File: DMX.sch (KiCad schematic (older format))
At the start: 7 parts, among them U10 ST485CDR

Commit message: Replaced the 10k-Resistor with one that is in stock
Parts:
- R25, R26: Buy https://www.digikey.com/product-detail/en/yageo/RC0603FR-07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 -> https://www.digikey.com/product-detail/en/bourns-inc/CR0603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
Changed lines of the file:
@@
 F 2 "Resistor_SMD:R_0603_1608Metric" V 980 2650 50  0001 C CNN
 F 3 "" H 1050 2650 50  0001 C CNN
-F 4 "https://www.digikey.com/product-detail/en/yageo/RC0603FR-0710KL/311-10.0KHRCT-ND/729827" V 1050 2650 50  0001 C CNN "Buy"
+F 4 "https://www.digikey.com/product-detail/en/bourns-inc/CR0603-FX-1002HLF/CR0603-FX-1002HLFCT-ND/3925297" V 1050 2650 50  0001 C CNN "Buy"
 	1    1050 2650
 	1    0    0    -1
@@
 F 2 "Resistor_SMD:R_0603_1608Metric" V 1680 2650 50  0001 C CNN
 F 3 "" H 1750 2650 50  0001 C CNN
-F 4 "https://www.digikey.com/product-detail/en/yageo/RC0603FR-0710KL/311-10.0KHRCT-ND/729827" V 1750 2650 50  0001 C CNN "Buy"
+F 4 "https://www.digikey.com/product-detail/en/bourns-inc/CR0603-FX-1002HLF/CR0603-FX-1002HLFCT-ND/3925297" V 1750 2650 50  0001 C CNN "Buy"
 	1    1750 2650
 	1    0    0    -1

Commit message: Replaced the 100nF Low-Voltage-Caps with one, which is still in stock
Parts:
- C34: Buy https://www.digikey.com/product-detail/en/kemet/C0603C104K3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 -> https://www.digikey.com/product-detail/en/murata-electronic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
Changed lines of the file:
@@
 F 2 "Capacitor_SMD:C_0603_1608Metric" H 2400 1400 50  0001 C CNN
 F 3 "" H 2400 1400 50  0001 C CNN
-F 4 "https://www.digikey.com/product-detail/en/kemet/C0603C104K3RACTU/399-1281-1-ND/416057" V 2400 1400 50  0001 C CNN "Buy"
+F 4 "https://www.digikey.com/product-detail/en/murata-electronics-north-america/GCM188R71C104KA37D/490-4774-1-ND/1641693" V 2400 1400 50  0001 C CNN "Buy"
 	1    2400 1400
 	0    1    1    0

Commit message: Removed the LV-Caps with the HV-Caps to remain consistent
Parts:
- C34: footprint Capacitor_SMD:C_0603_1608Metric -> Capacitor_SMD:C_0805_2012Metric; Buy https://www.digikey.com/product-detail/en/murata-electronics-north-america/GCM188R71C104KA37D/490-4774-1-ND/1641693 -> https://www.digikey.com/product-detail/en/murata-electronics-north-america/GCM21BR72A104KA37L/490-4789-1-ND/1641708
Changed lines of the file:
@@
 F 0 "C34" V 2500 1350 50  0000 L CNN
 F 1 "100nF" V 2300 1300 50  0000 L CNN
-F 2 "Capacitor_SMD:C_0603_1608Metric" H 2400 1400 50  0001 C CNN
+F 2 "Capacitor_SMD:C_0805_2012Metric" H 2400 1400 50  0001 C CNN
 F 3 "" H 2400 1400 50  0001 C CNN
-F 4 "https://www.digikey.com/product-detail/en/murata-electronics-north-america/GCM188R71C104KA37D/490-4774-1-ND/1641693" V 2400 1400 50  0001 C CNN "Buy"
+F 4 "https://www.digikey.com/product-detail/en/murata-electronics-north-america/GCM21BR72A104KA37L/490-4789-1-ND/1641708" V 2400 1400 50  0001 C CNN "Buy"
 	1    2400 1400
 	0    1    1    0

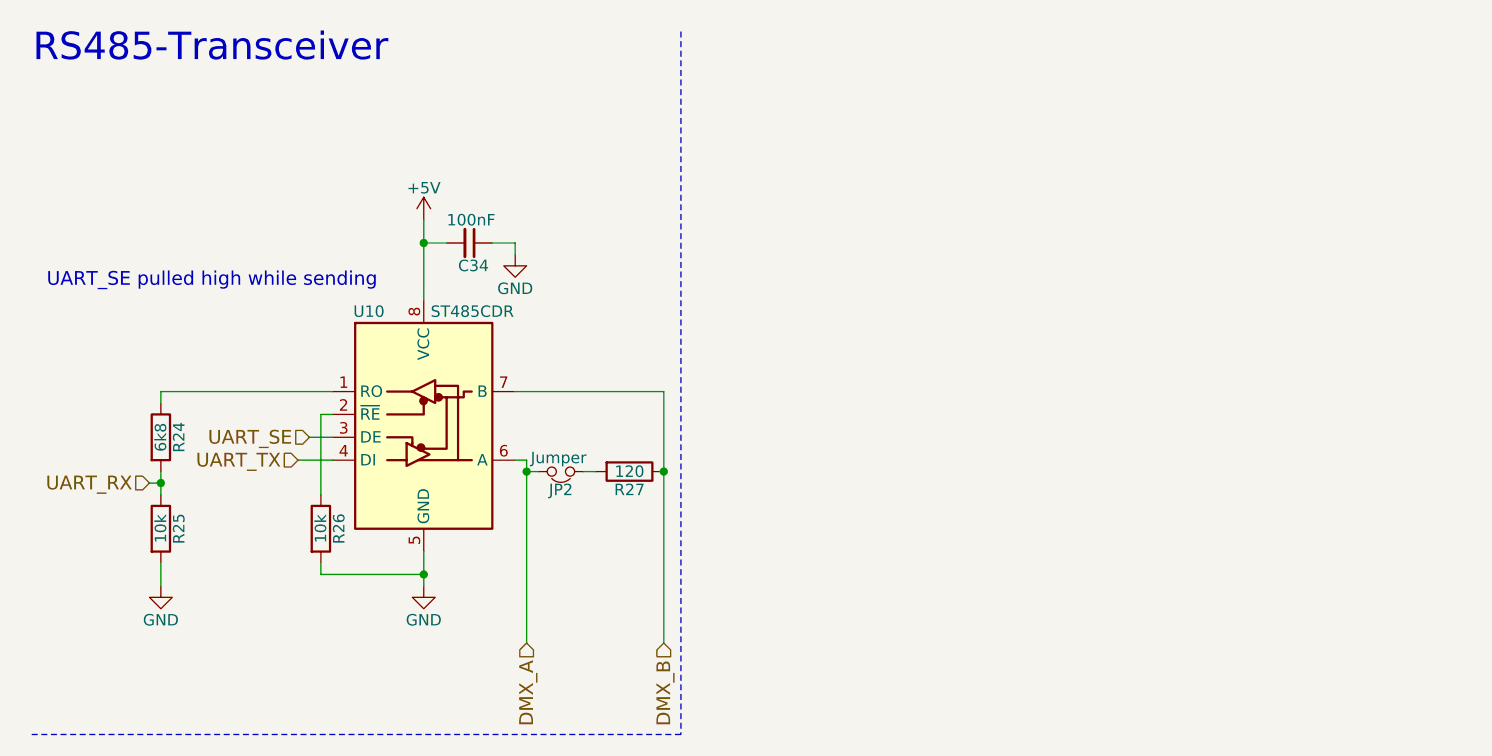
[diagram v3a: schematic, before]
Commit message: Added Address-Selector
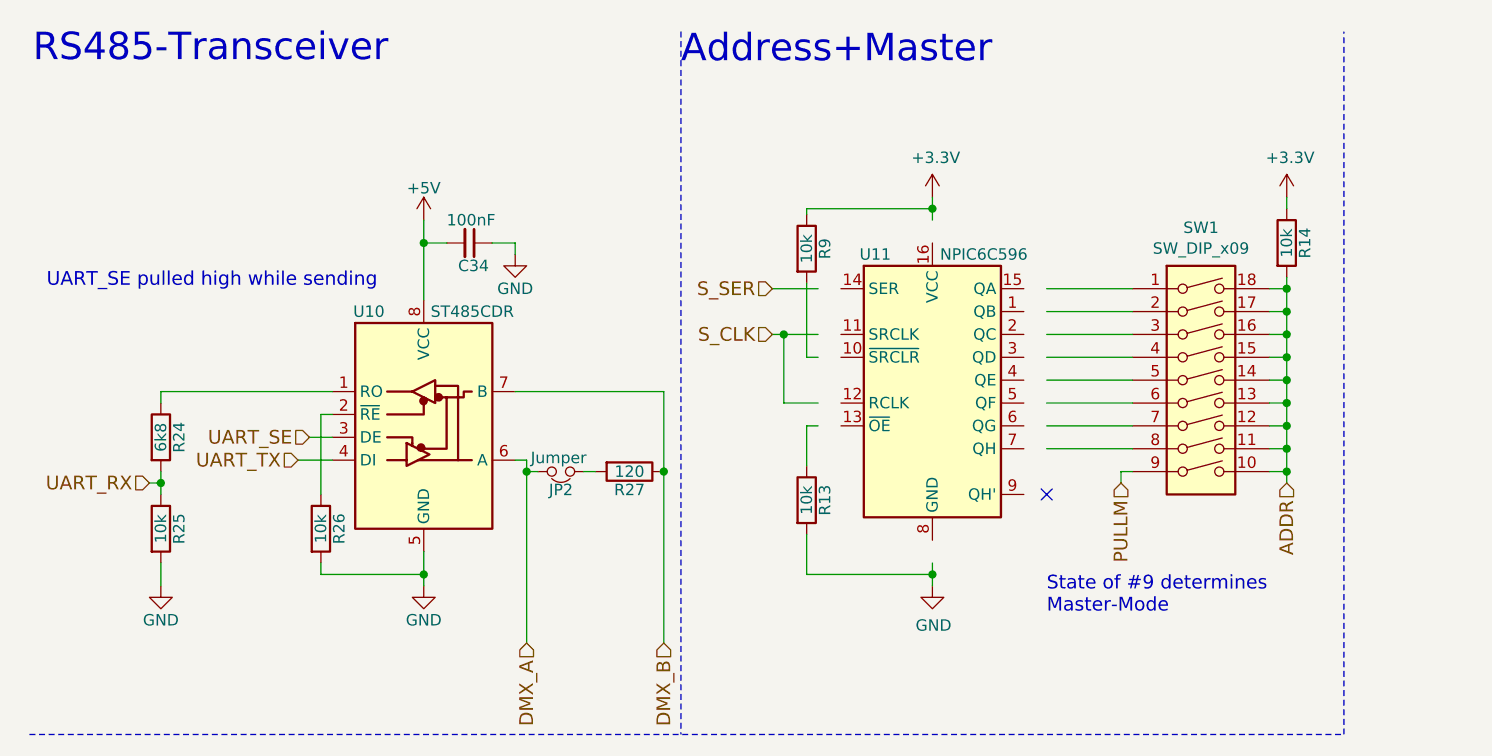
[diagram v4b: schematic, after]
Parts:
- added R13, R14, R9: 10k, Resistor_SMD:R_0603_1608Metric, symbol Device:R
- added SW1: SW_DIP_x09, Button_Switch_THT:SW_DIP_SPSTx09_Slide_9.78x25.04mm_W7.62mm_P2.54mm, symbol Switch:SW_DIP_x09
- added U11: NPIC6C596, Package_SO:SOIC-16_3.9x9.9mm_P1.27mm, symbol 74xx:74LS596
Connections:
- net labels added: +3.3V, ADDR, PULLM, S_CLK, S_SER
- wire segments 27 -> 74
- no-connect marks 0 -> 1
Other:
- note added: "Address+Master"
- note added: "State of #9 determines \nMaster-Mode"
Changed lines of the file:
@@
 Wire Notes Line
 	3325 475  3325 3550
-Wire Notes Line
-	3325 3550 475  3550
 Text HLabel 1000 2450 0    60   Input ~ 0
 UART_RX
@@
 Wire Wire Line
 	3250 2400 3250 3150
+$Comp
+L 74xx:74LS596 U11
+U 1 1 5B606C69
+P 4425 2000
+F 0 "U11" H 4175 2550 50  0000 C CNN
+F 1 "NPIC6C596" H 4650 2550 50  0000 C CNN
+F 2 "Package_SO:SOIC-16_3.9x9.9mm_P1.27mm" H 4425 2000 50  0001 C CNN
+F 3 "http://www.ti.com/lit/gpn/sn74ls596" H 4425 2000 50  0001 C CNN
+F 4 "https://www.digikey.com/product-detail/en/nexperia-usa-inc/NPIC6C596ADJ/1727-1846-1-ND" H 4425 2000 50  0001 C CNN "Buy"
+	1    4425 2000
+	1    0    0    -1
+$EndComp
+$Comp
+L power:+3.3V #PWR0108
+U 1 1 5B606E28
+P 4425 1200
+F 0 "#PWR0108" H 4425 1050 50  0001 C CNN
+F 1 "+3.3V" H 4440 1373 50  0000 C CNN
+F 2 "" H 4425 1200 50  0001 C CNN
+F 3 "" H 4425 1200 50  0001 C CNN
+	1    4425 1200
+	1    0    0    -1
+$EndComp
+Wire Wire Line
+	4425 1250 4425 1300
+$Comp
+L power:GND #PWR0109
+U 1 1 5B60719B
+P 4425 2900
+F 0 "#PWR0109" H 4425 2650 50  0001 C CNN
+F 1 "GND" H 4430 2727 50  0000 C CNN
+F 2 "" H 4425 2900 50  0001 C CNN
+F 3 "" H 4425 2900 50  0001 C CNN
+	1    4425 2900
+	1    0    0    -1
+$EndComp
+Wire Wire Line
+	4425 2850 4425 2800
+NoConn ~ 4925 2500
+$Comp
+L Switch:SW_DIP_x09 SW1
+U 1 1 5B607F5C
+P 5600 2000
+F 0 "SW1" H 5600 2667 50  0000 C CNN
+F 1 "SW_DIP_x09" H 5600 2576 50  0000 C CNN
+F 2 "Button_Switch_THT:SW_DIP_SPSTx09_Slide_9.78x25.04mm_W7.62mm_P2.54mm" H 5600 2000 50  0001 C CNN
+F 3 "" H 5600 2000 50  0001 C CNN
+F 4 "https://www.mouser.de/ProductDetail/CTS-Electronic-Components/208-9?qs=sGAEpiMZZMv%2f%252b2JhlA6ysHQcghgNQprpyH0Hmu0C8KY%3d" H 5600 2000 50  0001 C CNN "Buy"
+	1    5600 2000
+	1    0    0    -1
+$EndComp
+Wire Wire Line
+	4925 1600 5300 1600
+Wire Wire Line
+	4925 1800 5300 1800
+Wire Wire Line
+	5300 1900 4925 1900
+Wire Wire Line
+	4925 2000 5300 2000
+Wire Wire Line
+	5300 2100 4925 2100
+Wire Wire Line
+	4925 2200 5300 2200
+Wire Wire Line
+	4925 2300 5300 2300
+Wire Wire Line
+	4925 1700 5300 1700
+Wire Wire Line
+	5975 1550 5975 1600
+Wire Wire Line
+	5975 1600 5900 1600
+Wire Wire Line
+	5975 1600 5975 1700
+Wire Wire Line
+	5975 1700 5900 1700
+Connection ~ 5975 1600
+Wire Wire Line
+	5975 1700 5975 1800
+Wire Wire Line
+	5975 1800 5900 1800
+Connection ~ 5975 1700
+Wire Wire Line
+	5975 1800 5975 1900
+Wire Wire Line
+	5975 1900 5900 1900
+Connection ~ 5975 1800
+Wire Wire Line
+	5900 2000 5975 2000
+Wire Wire Line
+	5975 2000 5975 1900
+Connection ~ 5975 1900
+Wire Wire Line
+	5975 2000 5975 2100
+Wire Wire Line
+	5975 2100 5900 2100
+Connection ~ 5975 2000
+Wire Wire Line
+	5900 2200 5975 2200
+Wire Wire Line
+	5975 2200 5975 2100
+Connection ~ 5975 2100
+Wire Wire Line
+	5975 2200 5975 2300
+Wire Wire Line
+	5975 2300 5900 2300
+Connection ~ 5975 2200
+Wire Wire Line
+	5900 2400 5975 2400
+Wire Wire Line
+	5975 2400 5975 2300
+Connection ~ 5975 2300
+$Comp
+L power:+3.3V #PWR0110
+U 1 1 5B60F84C
+P 5975 1200
+F 0 "#PWR0110" H 5975 1050 50  0001 C CNN
+F 1 "+3.3V" H 5990 1373 50  0000 C CNN
+F 2 "" H 5975 1200 50  0001 C CNN
+F 3 "" H 5975 1200 50  0001 C CNN
+	1    5975 1200
+	1    0    0    -1
+$EndComp
+$Comp
+L Device:R R14
+U 1 1 5B61165A
+P 5975 1400
+F 0 "R14" V 6055 1400 50  0000 C CNN
+F 1 "10k" V 5975 1400 50  0000 C CNN
+F 2 "Resistor_SMD:R_0603_1608Metric" V 5905 1400 50  0001 C CNN
+F 3 "" H 5975 1400 50  0001 C CNN
+F 4 "https://www.digikey.com/product-detail/en/bourns-inc/CR0603-FX-1002HLF/CR0603-FX-1002HLFCT-ND/3925297" V 5975 1400 50  0001 C CNN "Buy"
+	1    5975 1400
+	1    0    0    -1
+$EndComp
+$Comp
+L Device:R R13
+U 1 1 5B611B4A
+P 3875 2525
+F 0 "R13" V 3955 2525 50  0000 C CNN
+F 1 "10k" V 3875 2525 50  0000 C CNN
+F 2 "Resistor_SMD:R_0603_1608Metric" V 3805 2525 50  0001 C CNN
+F 3 "" H 3875 2525 50  0001 C CNN
+F 4 "https://www.digikey.com/product-detail/en/bourns-inc/CR0603-FX-1002HLF/CR0603-FX-1002HLFCT-ND/3925297" V 3875 2525 50  0001 C CNN "Buy"
+	1    3875 2525
+	1    0    0    -1
+$EndComp
+Wire Wire Line
+	3875 2375 3875 2200
+Wire Wire Line
+	3875 2200 3925 2200
+$Comp
+L Device:R R9
+U 1 1 5B61520A
+P 3875 1425
+F 0 "R9" V 3955 1425 50  0000 C CNN
+F 1 "10k" V 3875 1425 50  0000 C CNN
+F 2 "Resistor_SMD:R_0603_1608Metric" V 3805 1425 50  0001 C CNN
+F 3 "" H 3875 1425 50  0001 C CNN
+F 4 "https://www.digikey.com/product-detail/en/bourns-inc/CR0603-FX-1002HLF/CR0603-FX-1002HLFCT-ND/3925297" V 3875 1425 50  0001 C CNN "Buy"
+	1    3875 1425
+	1    0    0    -1
+$EndComp
+Wire Wire Line
+	3875 1900 3875 1575
+Wire Wire Line
+	3875 2675 3875 2850
+Wire Wire Line
+	3875 1900 3925 1900
+Text HLabel 3725 1600 0    60   Input ~ 0
+S_SER
+Wire Wire Line
+	3725 1600 3925 1600
+Text HLabel 3725 1800 0    60   Input ~ 0
+S_CLK
+Wire Wire Line
+	3725 1800 3775 1800
+Wire Wire Line
+	3775 1800 3775 2100
+Wire Wire Line
+	3775 2100 3925 2100
+Connection ~ 3775 1800
+Wire Wire Line
+	3775 1800 3925 1800
+Text HLabel 5250 2450 3    60   Input ~ 0
+PULLM
+Wire Wire Line
+	5250 2450 5250 2400
+Wire Wire Line
+	5250 2400 5300 2400
+Text HLabel 5975 2450 3    60   Input ~ 0
+ADDR
+Wire Wire Line
+	5975 2450 5975 2400
+Connection ~ 5975 2400
+Wire Wire Line
+	3875 2850 4425 2850
+Connection ~ 4425 2850
+Wire Wire Line
+	3875 1275 3875 1250
+Wire Wire Line
+	3875 1250 4425 1250
+Connection ~ 4425 1250
+Wire Wire Line
+	4425 2850 4425 2900
+Wire Wire Line
+	4425 1200 4425 1250
+Wire Wire Line
+	5975 1200 5975 1250
+Text Notes 4925 3025 0    60   ~ 0
+State of #9 determines \nMaster-Mode
+Wire Notes Line
+	6225 3550 6225 475
+Wire Notes Line
+	475  3550 6225 3550
+Text Notes 3325 625  0    120  ~ 0
+Address+Master
 $EndSCHEMATC

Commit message: Filled in the Parts for the Fault-Indicator
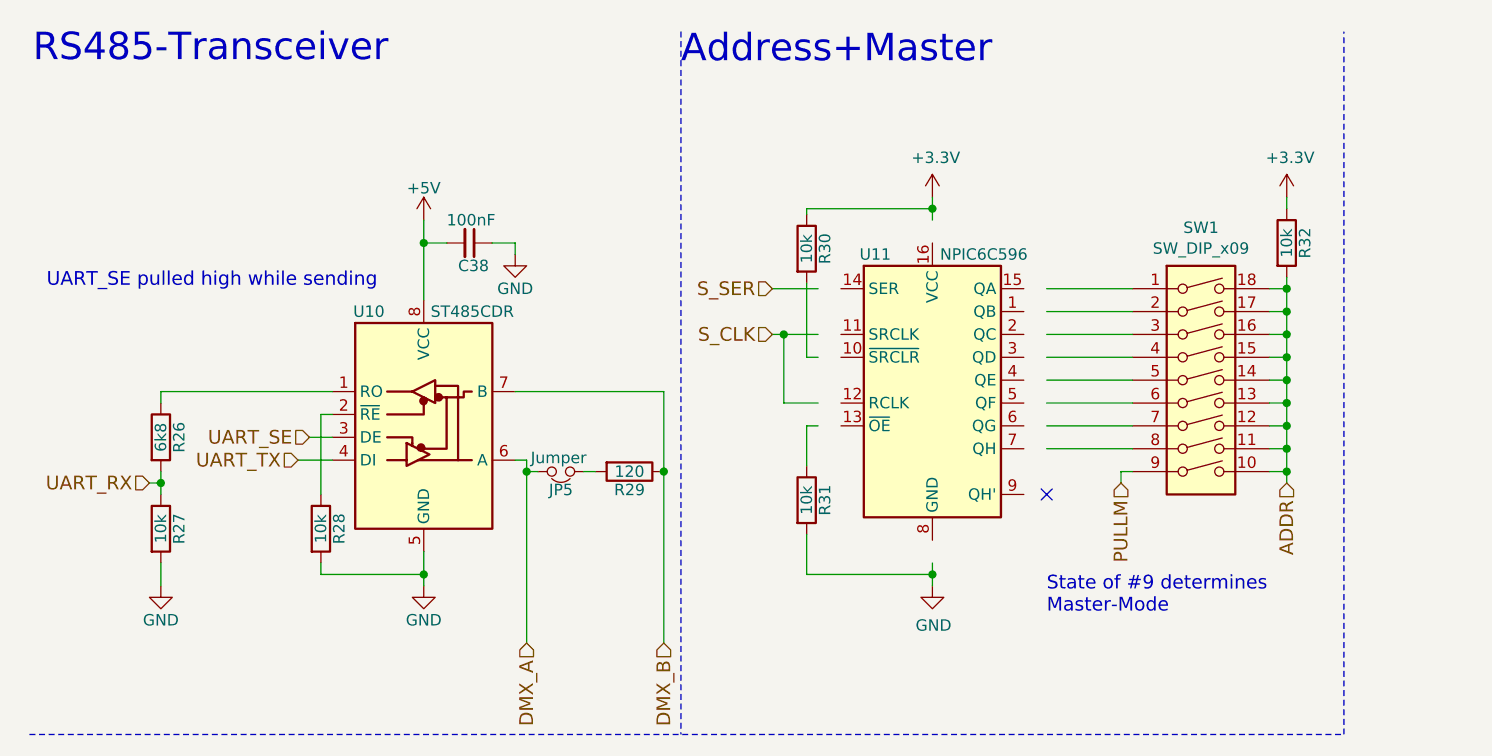
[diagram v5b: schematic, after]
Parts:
- renumbered C34 to C38, JP2 to JP5, R24 to R26, R25 to R27, R26 to R28, R27 to R29, R9 to R30, R13 to R31, R14 to R32
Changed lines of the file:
@@
 $EndComp
 $Comp
-L Device:C_Small C34
+L Device:C_Small C38
 U 1 1 5A847703
 P 2400 1400
-F 0 "C34" V 2500 1350 50  0000 L CNN
+F 0 "C38" V 2500 1350 50  0000 L CNN
 F 1 "100nF" V 2300 1300 50  0000 L CNN
 F 2 "Capacitor_SMD:C_0805_2012Metric" H 2400 1400 50  0001 C CNN
@@
 $EndComp
 $Comp
-L power:GND #PWR088
+L power:GND #PWR094
 U 1 1 5A84770A
 P 2600 1450
-F 0 "#PWR088" H 2600 1200 50  0001 C CNN
+F 0 "#PWR094" H 2600 1200 50  0001 C CNN
 F 1 "GND" H 2600 1300 50  0000 C CNN
 F 2 "" H 2600 1450 50  0001 C CNN
@@
 $EndComp
 $Comp
-L power:+5V #PWR086
+L power:+5V #PWR092
 U 1 1 5A847710
 P 2200 1300
-F 0 "#PWR086" H 2200 1150 50  0001 C CNN
+F 0 "#PWR092" H 2200 1150 50  0001 C CNN
 F 1 "+5V" H 2200 1440 50  0000 C CNN
 F 2 "" H 2200 1300 50  0001 C CNN
@@
 $EndComp
 $Comp
-L power:GND #PWR087
+L power:GND #PWR093
 U 1 1 5A847716
 P 2200 2900
-F 0 "#PWR087" H 2200 2650 50  0001 C CNN
+F 0 "#PWR093" H 2200 2650 50  0001 C CNN
 F 1 "GND" H 2200 2750 50  0000 C CNN
 F 2 "" H 2200 2900 50  0001 C CNN
@@
 $EndComp
 $Comp
-L Device:R R24
+L Device:R R26
 U 1 1 5A84771C
 P 1050 2250
-F 0 "R24" V 1130 2250 50  0000 C CNN
+F 0 "R26" V 1130 2250 50  0000 C CNN
 F 1 "6k8" V 1050 2250 50  0000 C CNN
 F 2 "Resistor_SMD:R_0603_1608Metric" V 980 2250 50  0001 C CNN
@@
 $EndComp
 $Comp
-L Device:R R25
+L Device:R R27
 U 1 1 5A847723
 P 1050 2650
-F 0 "R25" V 1130 2650 50  0000 C CNN
+F 0 "R27" V 1130 2650 50  0000 C CNN
 F 1 "10k" V 1050 2650 50  0000 C CNN
 F 2 "Resistor_SMD:R_0603_1608Metric" V 980 2650 50  0001 C CNN
@@
 $EndComp
 $Comp
-L power:GND #PWR085
+L power:GND #PWR091
 U 1 1 5A84772A
 P 1050 2900
-F 0 "#PWR085" H 1050 2650 50  0001 C CNN
+F 0 "#PWR091" H 1050 2650 50  0001 C CNN
 F 1 "GND" H 1050 2750 50  0000 C CNN
 F 2 "" H 1050 2900 50  0001 C CNN
@@
 $EndComp
 $Comp
-L Device:R R26
+L Device:R R28
 U 1 1 5A847733
 P 1750 2650
-F 0 "R26" V 1830 2650 50  0000 C CNN
+F 0 "R28" V 1830 2650 50  0000 C CNN
 F 1 "10k" V 1750 2650 50  0000 C CNN
 F 2 "Resistor_SMD:R_0603_1608Metric" V 1680 2650 50  0001 C CNN
@@
 UART_SE pulled high while sending
 $Comp
-L Device:R R27
+L Device:R R29
 U 1 1 5A847744
 P 3100 2400
-F 0 "R27" V 3180 2400 50  0000 C CNN
+F 0 "R29" V 3180 2400 50  0000 C CNN
 F 1 "120" V 3100 2400 50  0000 C CNN
 F 2 "Resistor_SMD:R_1206_3216Metric" V 3030 2400 50  0001 C CNN
@@
 $EndComp
 $Comp
-L Device:Jumper_NC_Small JP2
+L Device:Jumper_NC_Small JP5
 U 1 1 5A84774B
 P 2800 2400
-F 0 "JP2" H 2800 2480 50  0000 C CNN
+F 0 "JP5" H 2800 2480 50  0000 C CNN
 F 1 "Jumper" H 2810 2340 50  0000 C CNN
 F 2 "Connector_PinHeader_2.54mm:PinHeader_2x01_P2.54mm_Vertical" H 2800 2400 50  0001 C CNN
@@
 $EndComp
 $Comp
-L power:+3.3V #PWR0108
+L power:+3.3V #PWR095
 U 1 1 5B606E28
 P 4425 1200
-F 0 "#PWR0108" H 4425 1050 50  0001 C CNN
+F 0 "#PWR095" H 4425 1050 50  0001 C CNN
 F 1 "+3.3V" H 4440 1373 50  0000 C CNN
 F 2 "" H 4425 1200 50  0001 C CNN
@@
 	4425 1250 4425 1300
 $Comp
-L power:GND #PWR0109
+L power:GND #PWR096
 U 1 1 5B60719B
 P 4425 2900
-F 0 "#PWR0109" H 4425 2650 50  0001 C CNN
+F 0 "#PWR096" H 4425 2650 50  0001 C CNN
 F 1 "GND" H 4430 2727 50  0000 C CNN
 F 2 "" H 4425 2900 50  0001 C CNN
@@
 Connection ~ 5975 2300
 $Comp
-L power:+3.3V #PWR0110
+L power:+3.3V #PWR097
 U 1 1 5B60F84C
 P 5975 1200
-F 0 "#PWR0110" H 5975 1050 50  0001 C CNN
+F 0 "#PWR097" H 5975 1050 50  0001 C CNN
 F 1 "+3.3V" H 5990 1373 50  0000 C CNN
 F 2 "" H 5975 1200 50  0001 C CNN
@@
 $EndComp
 $Comp
-L Device:R R14
+L Device:R R32
 U 1 1 5B61165A
 P 5975 1400
-F 0 "R14" V 6055 1400 50  0000 C CNN
+F 0 "R32" V 6055 1400 50  0000 C CNN
 F 1 "10k" V 5975 1400 50  0000 C CNN
 F 2 "Resistor_SMD:R_0603_1608Metric" V 5905 1400 50  0001 C CNN
@@
 $EndComp
 $Comp
-L Device:R R13
+L Device:R R31
 U 1 1 5B611B4A
 P 3875 2525
-F 0 "R13" V 3955 2525 50  0000 C CNN
+F 0 "R31" V 3955 2525 50  0000 C CNN
 F 1 "10k" V 3875 2525 50  0000 C CNN
 F 2 "Resistor_SMD:R_0603_1608Metric" V 3805 2525 50  0001 C CNN
@@
 	3875 2200 3925 2200
 $Comp
-L Device:R R9
+L Device:R R30
 U 1 1 5B61520A
 P 3875 1425
-F 0 "R9" V 3955 1425 50  0000 C CNN
+F 0 "R30" V 3955 1425 50  0000 C CNN
 F 1 "10k" V 3875 1425 50  0000 C CNN
 F 2 "Resistor_SMD:R_0603_1608Metric" V 3805 1425 50  0001 C CNN
